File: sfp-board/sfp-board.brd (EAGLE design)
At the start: 107.6 x 80 mm, 22 parts

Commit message: Final board Arrangement #2
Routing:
- net GND: track 71.1 -> 65.0 mm
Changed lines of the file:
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@@
 <attribute name="NAME" x="50.927" y="57.15" size="1.27" layer="25" ratio="10" rot="R90"/>
 <attribute name="SPICEPREFIX" value="R" x="53.34" y="50.8" size="1.778" layer="27" rot="R90" display="off"/>
-<attribute name="VALUE" x="52.705" y="47.2186" size="1.27" layer="27" ratio="10" rot="R90"/>
+<attribute name="VALUE" x="53.975" y="51.0286" size="1.27" layer="27" ratio="10" rot="R90"/>
 </element>
 <element name="S1" library="diy-modules" package="TEMP-HUM-SENSOR-DHT11" value="DHT11" x="34.29" y="71.12" smashed="yes" rot="R270">
@@
 <contactref element="GP2Y1010AU0F" pad="2"/>
 <wire x1="20.32" y1="10.16" x2="35.56" y2="10.16" width="0.4064" layer="1"/>
-<wire x1="35.56" y1="10.16" x2="43.18" y2="17.78" width="0.4064" layer="1"/>
-<wire x1="43.18" y1="17.78" x2="45.72" y2="17.78" width="0.4064" layer="1"/>
-<wire x1="45.72" y1="17.78" x2="48.26" y2="20.32" width="0.4064" layer="1"/>
-<wire x1="48.26" y1="20.32" x2="53.34" y2="20.32" width="0.4064" layer="1"/>
-<wire x1="99.06" y1="58.42" x2="100.33" y2="58.42" width="0.4064" layer="1"/>
-<wire x1="100.33" y1="58.42" x2="102.87" y2="55.88" width="0.4064" layer="1"/>
-<wire x1="102.87" y1="55.88" x2="102.87" y2="52.07" width="0.4064" layer="1"/>
-<wire x1="102.87" y1="52.07" x2="100.33" y2="49.53" width="0.4064" layer="1"/>
-<wire x1="100.33" y1="49.53" x2="78.74" y2="49.53" width="0.4064" layer="1"/>
+<wire x1="35.56" y1="10.16" x2="45.72" y2="20.32" width="0.4064" layer="1"/>
+<wire x1="45.72" y1="20.32" x2="53.34" y2="20.32" width="0.4064" layer="1"/>
+<wire x1="99.06" y1="58.42" x2="97.79" y2="58.42" width="0.4064" layer="1"/>
+<wire x1="97.79" y1="58.42" x2="96.52" y2="57.15" width="0.4064" layer="1"/>
+<wire x1="96.52" y1="57.15" x2="96.52" y2="50.8" width="0.4064" layer="1"/>
+<wire x1="96.52" y1="50.8" x2="95.25" y2="49.53" width="0.4064" layer="1"/>
+<wire x1="95.25" y1="49.53" x2="78.74" y2="49.53" width="0.4064" layer="1"/>
 <via x="78.74" y="49.53" extent="1-16" drill="0.6" shape="square"/>
 </signal>

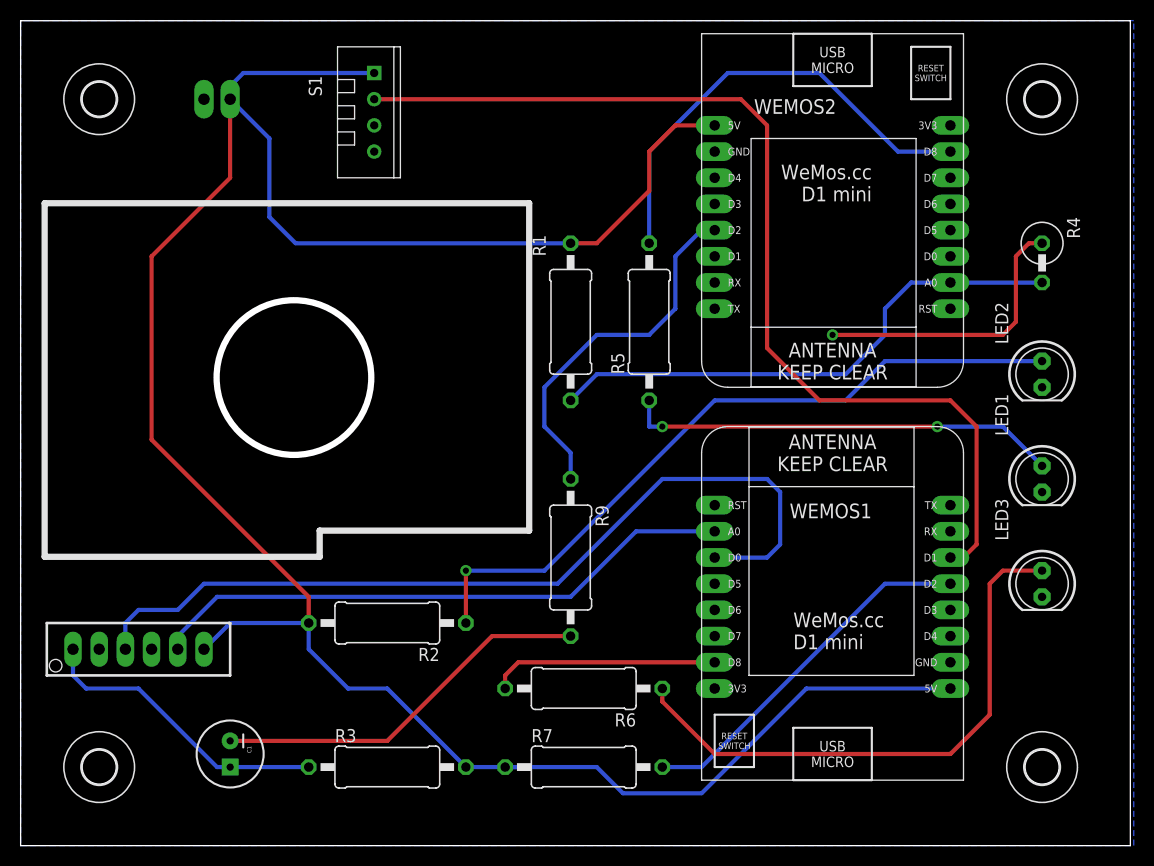
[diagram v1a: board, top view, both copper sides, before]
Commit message: Final board arrangement
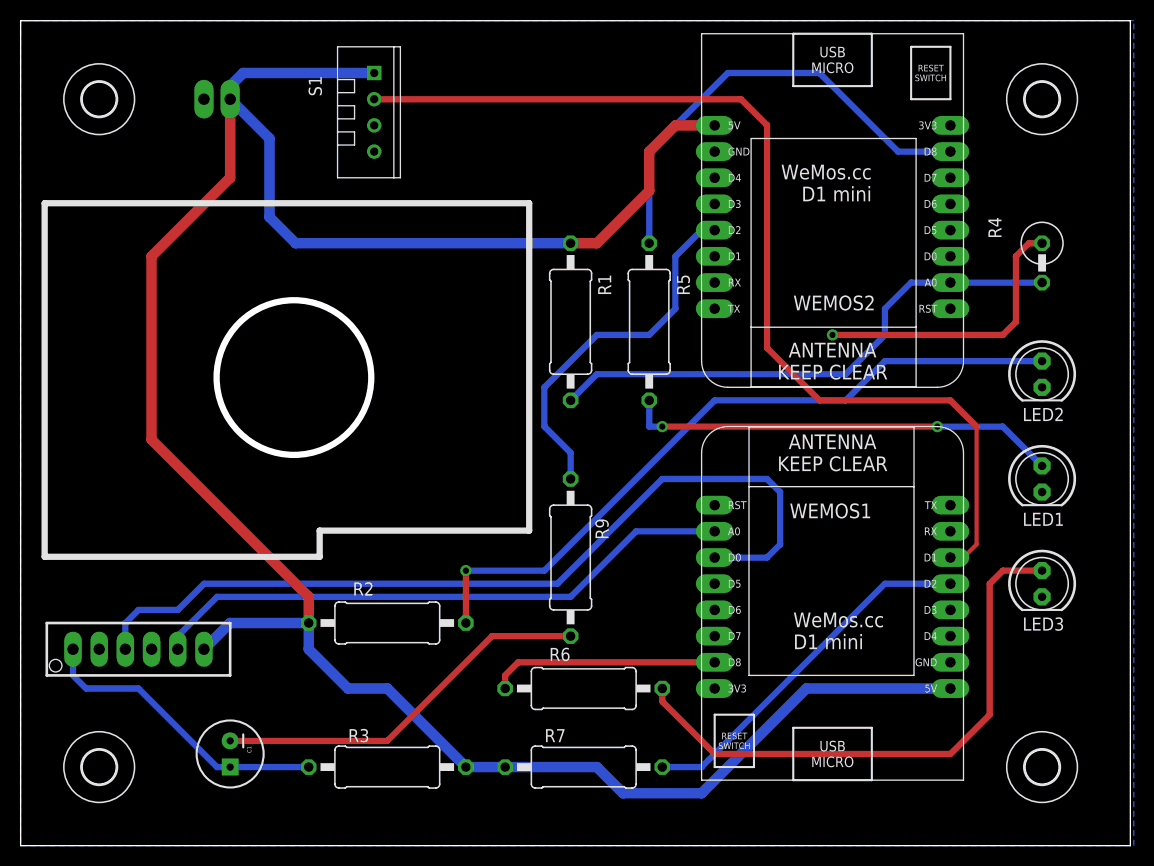
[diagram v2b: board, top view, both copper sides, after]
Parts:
- moved U$1 38.6 mm to (38.1, 57.1)

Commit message: Final Board arrangement #4
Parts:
- LED1, LED2, LED3: device adafruit:LED5MM -> digital-toy:LED5MM
- R1, R2, R3, R5, R6, R7, R9: device rcl:0411/15 -> digital-toy:0414/15
- R4: device rcl:0411V -> digital-toy:0414V
- moved R4 1.27 mm to (99.1, 57.1)
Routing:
- net GND: track 65.0 -> 65.5 mm
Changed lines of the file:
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@@
 </autorouter>
 <elements>
-<element name="R1" library="rcl" package="0411/15" value="100k" x="53.34" y="50.8" smashed="yes" rot="R90">
+<element name="R1" library="digital-toy" package="0414/15" value="100k" x="53.34" y="50.8" smashed="yes" rot="R90">
 <attribute name="NAME" x="57.277" y="53.34" size="1.27" layer="25" ratio="10" rot="R90"/>
-<attribute name="SPICEPREFIX" value="R" x="53.34" y="50.8" size="1.778" layer="27" rot="R90" display="off"/>
 <attribute name="VALUE" x="53.975" y="51.0286" size="1.27" layer="27" ratio="10" rot="R90"/>
 </element>
@@
 <element name="H3" library="holes" package="3,3" value="MOUNT-HOLE3.3" x="99.06" y="7.62"/>
 <element name="H4" library="holes" package="3,3" value="MOUNT-HOLE3.3" x="7.62" y="7.62"/>
-<element name="R4" library="rcl" package="0411V" value="Photoresistor" x="99.06" y="55.88" smashed="yes" rot="R270">
-<attribute name="SPICEPREFIX" value="R" x="99.06" y="55.88" size="1.778" layer="27" rot="R270" display="off"/>
-<attribute name="NAME" x="93.853" y="60.96" size="1.27" layer="25" ratio="10" rot="R270"/>
-<attribute name="VALUE" x="102.235" y="64.5414" size="1.27" layer="27" ratio="10" rot="R270"/>
+<element name="R4" library="digital-toy" package="0414V" value="Photoresistor" x="99.06" y="57.15" smashed="yes" rot="R270">
+<attribute name="NAME" x="93.853" y="62.23" size="1.27" layer="25" ratio="10" rot="R270"/>
+<attribute name="VALUE" x="102.235" y="65.8114" size="1.27" layer="27" ratio="10" rot="R270"/>
 </element>
-<element name="LED1" library="adafruit" package="LED5MM" value="status 2" x="99.06" y="35.56" smashed="yes" rot="R270">
+<element name="LED1" library="digital-toy" package="LED5MM" value="status 2" x="99.06" y="35.56" smashed="yes" rot="R270">
 <attribute name="NAME" x="97.155" y="31.0134" size="1.27" layer="25" ratio="10"/>
 <attribute name="VALUE" x="103.6066" y="39.9796" size="1.27" layer="27" ratio="10" rot="R270"/>
 </element>
-<element name="LED2" library="adafruit" package="LED5MM" value="power" x="99.06" y="45.72" smashed="yes" rot="R270">
+<element name="LED2" library="digital-toy" package="LED5MM" value="power" x="99.06" y="45.72" smashed="yes" rot="R270">
 <attribute name="NAME" x="97.155" y="41.1734" size="1.27" layer="25" ratio="10"/>
 <attribute name="VALUE" x="103.6066" y="48.8696" size="1.27" layer="27" ratio="10" rot="R270"/>
 </element>
-<element name="LED3" library="adafruit" package="LED5MM" value="status 1" x="99.06" y="25.4" smashed="yes" rot="R270">
+<element name="LED3" library="digital-toy" package="LED5MM" value="status 1" x="99.06" y="25.4" smashed="yes" rot="R270">
 <attribute name="NAME" x="97.155" y="20.8534" size="1.27" layer="25" ratio="10"/>
 <attribute name="VALUE" x="103.6066" y="28.5496" size="1.27" layer="27" ratio="10" rot="R270"/>
 </element>
-<element name="R2" library="rcl" package="0411/15" value="1k" x="35.56" y="21.59" smashed="yes" rot="R180">
-<attribute name="SPICEPREFIX" value="R" x="35.56" y="21.59" size="1.778" layer="27" rot="R180" display="off"/>
+<element name="R2" library="digital-toy" package="0414/15" value="1k" x="35.56" y="21.59" smashed="yes" rot="R180">
 <attribute name="NAME" x="34.29" y="25.527" size="1.27" layer="25" ratio="10" rot="R180"/>
 <attribute name="VALUE" x="34.0614" y="22.225" size="1.27" layer="27" ratio="10" rot="R180"/>
 </element>
-<element name="R5" library="rcl" package="0411/15" value="470" x="60.96" y="50.8" smashed="yes" rot="R90">
-<attribute name="SPICEPREFIX" value="R" x="60.96" y="50.8" size="1.778" layer="27" rot="R90" display="off"/>
+<element name="R5" library="digital-toy" package="0414/15" value="470" x="60.96" y="50.8" smashed="yes" rot="R90">
 <attribute name="NAME" x="64.897" y="53.34" size="1.27" layer="25" ratio="10" rot="R90"/>
 <attribute name="VALUE" x="61.595" y="51.0286" size="1.27" layer="27" ratio="10" rot="R90"/>
 </element>
-<element name="R6" library="rcl" package="0411/15" value="470" x="54.61" y="15.24" smashed="yes" rot="R180">
-<attribute name="SPICEPREFIX" value="R" x="54.61" y="15.24" size="1.778" layer="27" rot="R180" display="off"/>
+<element name="R6" library="digital-toy" package="0414/15" value="470" x="54.61" y="15.24" smashed="yes" rot="R180">
 <attribute name="NAME" x="53.34" y="19.177" size="1.27" layer="25" ratio="10" rot="R180"/>
 <attribute name="VALUE" x="54.3814" y="15.875" size="1.27" layer="27" ratio="10" rot="R180"/>
 </element>
-<element name="R7" library="rcl" package="0411/15" value="10k" x="54.61" y="7.62" smashed="yes">
-<attribute name="SPICEPREFIX" value="R" x="54.61" y="7.62" size="1.778" layer="27" display="off"/>
+<element name="R7" library="digital-toy" package="0414/15" value="10k" x="54.61" y="7.62" smashed="yes">
 <attribute name="NAME" x="50.8" y="10.033" size="1.27" layer="25" ratio="10"/>
 <attribute name="VALUE" x="51.0286" y="6.985" size="1.27" layer="27" ratio="10"/>
 </element>
-<element name="R9" library="rcl" package="0411/15" value="10k" x="53.34" y="27.94" smashed="yes" rot="R270">
-<attribute name="SPICEPREFIX" value="R" x="53.34" y="27.94" size="1.778" layer="27" rot="R270" display="off"/>
+<element name="R9" library="digital-toy" package="0414/15" value="10k" x="53.34" y="27.94" smashed="yes" rot="R270">
 <attribute name="NAME" x="55.753" y="31.75" size="1.27" layer="25" ratio="10" rot="R270"/>
 <attribute name="VALUE" x="52.705" y="31.5214" size="1.27" layer="27" ratio="10" rot="R270"/>
@@
 <attribute name="NAME" x="21.971" y="9.652" size="0.4064" layer="25" rot="R270"/>
 </element>
-<element name="R3" library="rcl" package="0411/15" value="150" x="35.56" y="7.62" smashed="yes">
-<attribute name="SPICEPREFIX" value="R" x="35.56" y="7.62" size="1.778" layer="27" display="off"/>
+<element name="R3" library="digital-toy" package="0414/15" value="150" x="35.56" y="7.62" smashed="yes">
 <attribute name="NAME" x="31.75" y="10.033" size="1.27" layer="25" ratio="10"/>
 <attribute name="VALUE" x="31.9786" y="6.985" size="1.27" layer="27" ratio="10"/>
@@
 <wire x1="35.56" y1="10.16" x2="45.72" y2="20.32" width="0.6096" layer="1"/>
 <wire x1="45.72" y1="20.32" x2="53.34" y2="20.32" width="0.6096" layer="1"/>
-<wire x1="99.06" y1="58.42" x2="97.79" y2="58.42" width="0.6096" layer="1"/>
-<wire x1="97.79" y1="58.42" x2="96.52" y2="57.15" width="0.6096" layer="1"/>
+<wire x1="99.06" y1="59.69" x2="96.52" y2="57.15" width="0.6096" layer="1"/>
 <wire x1="96.52" y1="57.15" x2="96.52" y2="50.8" width="0.6096" layer="1"/>
 <wire x1="96.52" y1="50.8" x2="95.25" y2="49.53" width="0.6096" layer="1"/>
